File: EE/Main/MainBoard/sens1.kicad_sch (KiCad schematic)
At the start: 3 parts, among them J2 Conn_02x13_Odd_Even

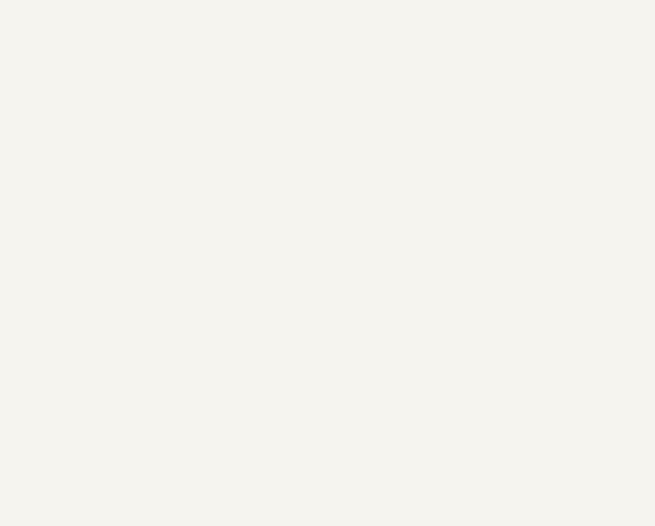
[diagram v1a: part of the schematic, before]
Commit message: WIP - Moving Sensor to IO Expander
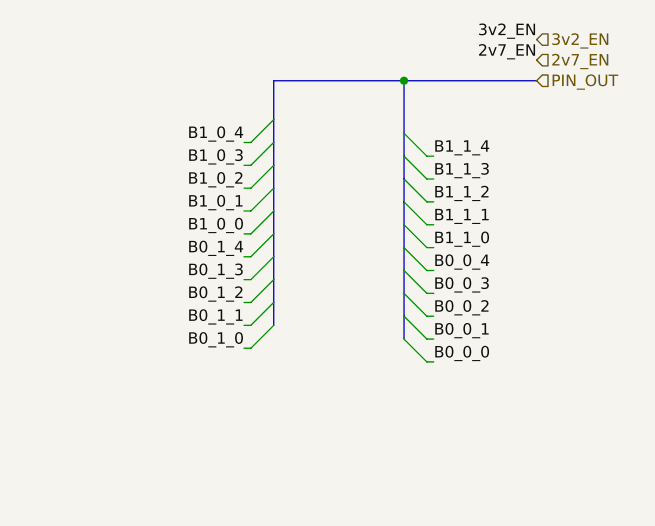
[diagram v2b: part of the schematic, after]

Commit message: Updated layout, and placement for main board
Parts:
- removed J2: Conn_02x13_Odd_Even, Connector_PinHeader_1.27mm:PinHeader_2x13_P1.27mm_Vertical_SMD, symbol Connector_Generic:Conn_02x13_Odd_Even
- added J2: Conn_01x04_Male, Connector_PinSocket_2.54mm:PinSocket_1x04_P2.54mm_Vertical, symbol Connector:Conn_01x04_Male
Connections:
- net GND: now also J2.4 (Pin_4)
- net VCC: now also J2.1 (Pin_1)
- new net SCL: J2.2 (Pin_2)
- new net SDA: J2.3 (Pin_3)
- no-connect marks 2 -> 0

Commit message: Routine Update
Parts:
- H3, H4: footprint MountingHole:MountingHole_2.5mm -> MountingHole:MountingHole_2.7mm
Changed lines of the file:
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@@
       (effects (font (size 1.27 1.27)) (justify left))
     )
-    (property "Footprint" "MountingHole:MountingHole_2.5mm" (id 2) (at 122.936 106.426 0)
+    (property "Footprint" "MountingHole:MountingHole_2.7mm" (id 2) (at 122.936 106.426 0)
       (effects (font (size 1.27 1.27)) hide)
     )
@@
       (effects (font (size 1.27 1.27)) (justify left))
     )
-    (property "Footprint" "MountingHole:MountingHole_2.5mm" (id 2) (at 122.936 62.23 0)
+    (property "Footprint" "MountingHole:MountingHole_2.7mm" (id 2) (at 122.936 62.23 0)
       (effects (font (size 1.27 1.27)) hide)
     )
